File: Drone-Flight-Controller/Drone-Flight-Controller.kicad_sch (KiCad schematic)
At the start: 58 parts, among them J1 Screw_Terminal_01x02, J10 Conn_ARM_SWD_TagConnect_TC203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, J2 USB_B_Micro, J3 Screw_Terminal_01x03, J4 Screw_Terminal_01x03, J5 Screw_Terminal_01x03, J6 Screw_Terminal_01x03, J7 Screw_Terminal_01x02, J8 Screw_Terminal_01x03, SW1 SW_SPDT, U1 LMR51430, U2 NCP1117-3.3_SOT223, U3 STM32F401CBUx, U4 USBLC6-2SC6, U5 ADC101C021CIMK, U6 MPU-6050, U7 BMP280, Y1 16MHz

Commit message: forgot to save
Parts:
- removed H1, H2, H3, H4: MountingHole_Pad, MountingHole:MountingHole_4.3mm_M4_Pad_Via, symbol Mechanical:MountingHole_Pad
- removed SW1: SW_SPDT, Button_Switch_SMD:SW_SPDT_PCM12, symbol Switch:SW_SPDT
- added D2: LED, LED_SMD:LED_0402_1005Metric, symbol Device:LED
- added TP10, TP11, TP12, TP13, TP2, TP3, TP4, TP5, TP6, TP7, TP8, TP9: TestPoint, TestPoint:TestPoint_Pad_D1.0mm, symbol Connector:TestPoint
- C10: footprint Capacitor_THT:C_Radial_D4.0mm_H5.0mm_P1.50mm -> Capacitor_SMD:C_0504_1310Metric
- C2, C22, C23, C7: footprint Capacitor_THT:C_Radial_D4.0mm_H5.0mm_P1.50mm -> Capacitor_SMD:C_0402_1005Metric
- D1: footprint LED_THT:LED_D3.0mm -> LED_SMD:LED_0402_1005Metric
- D3: renamed from D2; footprint LED_THT:LED_D3.0mm -> LED_SMD:LED_0402_1005Metric
- R2, R3, R4, R5, R6, R7: footprint Resistor_THT:R_Axial_DIN0204_L3.6mm_D1.6mm_P7.62mm_Horizontal -> Resistor_SMD:R_0402_1005Metric
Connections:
- net +3.3V: now also R10.1
- net +5V: now also D2.2 (A)
- net BATVOLTAGE_ADDR: now also U3.31 (PA10)
- net BATVOLTAGE_SCL: now also U3.29 (PA8)
- net BATVOLTAGE_SDA: now also U3.30 (PA9)
- net GND: now also D2.1 (K)
- net SWCLK: now also J10.4 (SWCLK); no longer J10.2 (SWDIO)
- net SWDIO: now also J10.2 (SWDIO); no longer J10.4 (SWCLK)
- net UART_RX: now also J8.2 (Pin_2); no longer J8.3 (Pin_3)
- net UART_TX: now also J8.3 (Pin_3); no longer J8.2 (Pin_2)
- net at U3.18 (PB0): now also TP3.1
- net at U3.19 (PB1): now also TP4.1
- net at U3.2 (PC13): now also TP12.1
- net at U3.20 (PB2): now also TP5.1
- net at U3.21 (PB10): now also TP11.1
- net at U3.25 (PB12): now also TP10.1
- net at U3.26 (PB13): now also TP9.1
- net at U3.27 (PB14): now also TP8.1
- net at U3.28 (PB15): now also TP7.1
- net at U3.3 (PC14): now also TP13.1
- net at U3.38 (PA15): now also TP2.1
- net at U3.41 (PB5): now also TP6.1
- no-connect marks 7 -> 2

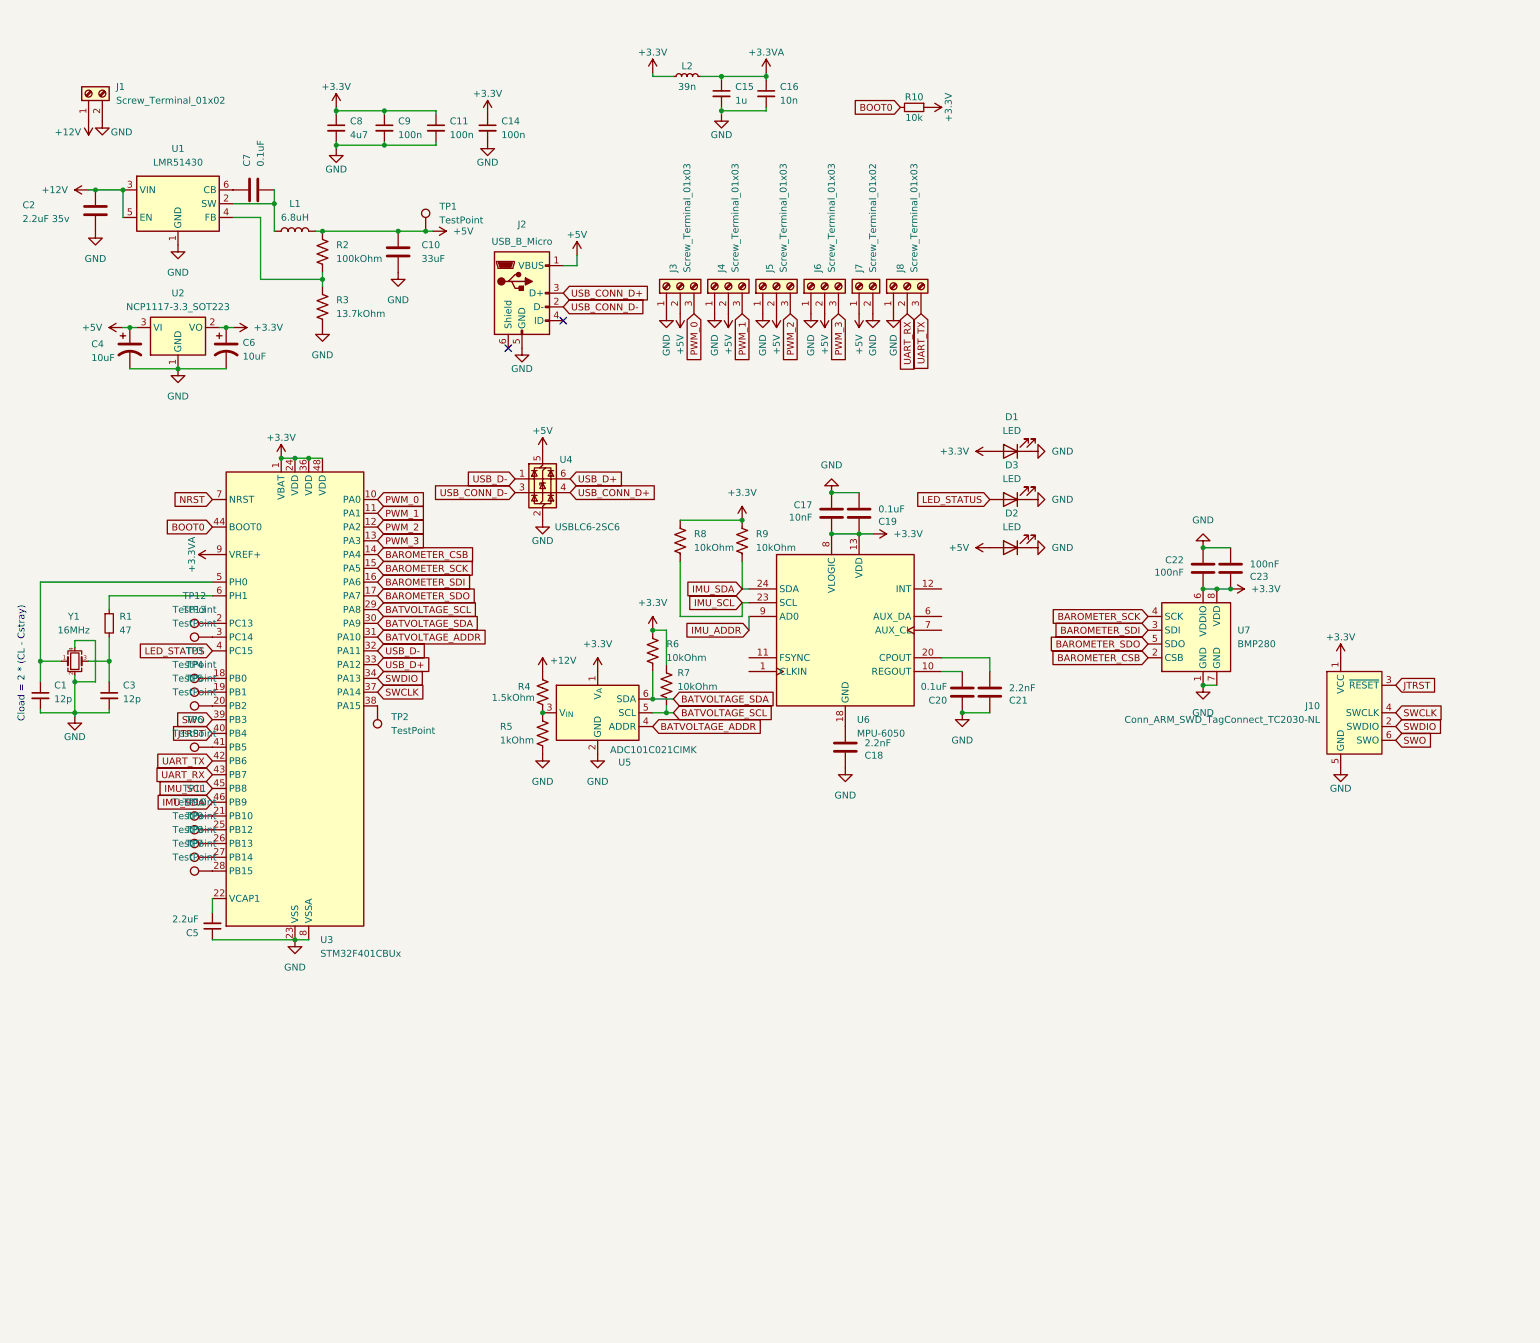
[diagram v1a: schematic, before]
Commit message: move to more powerful mcu
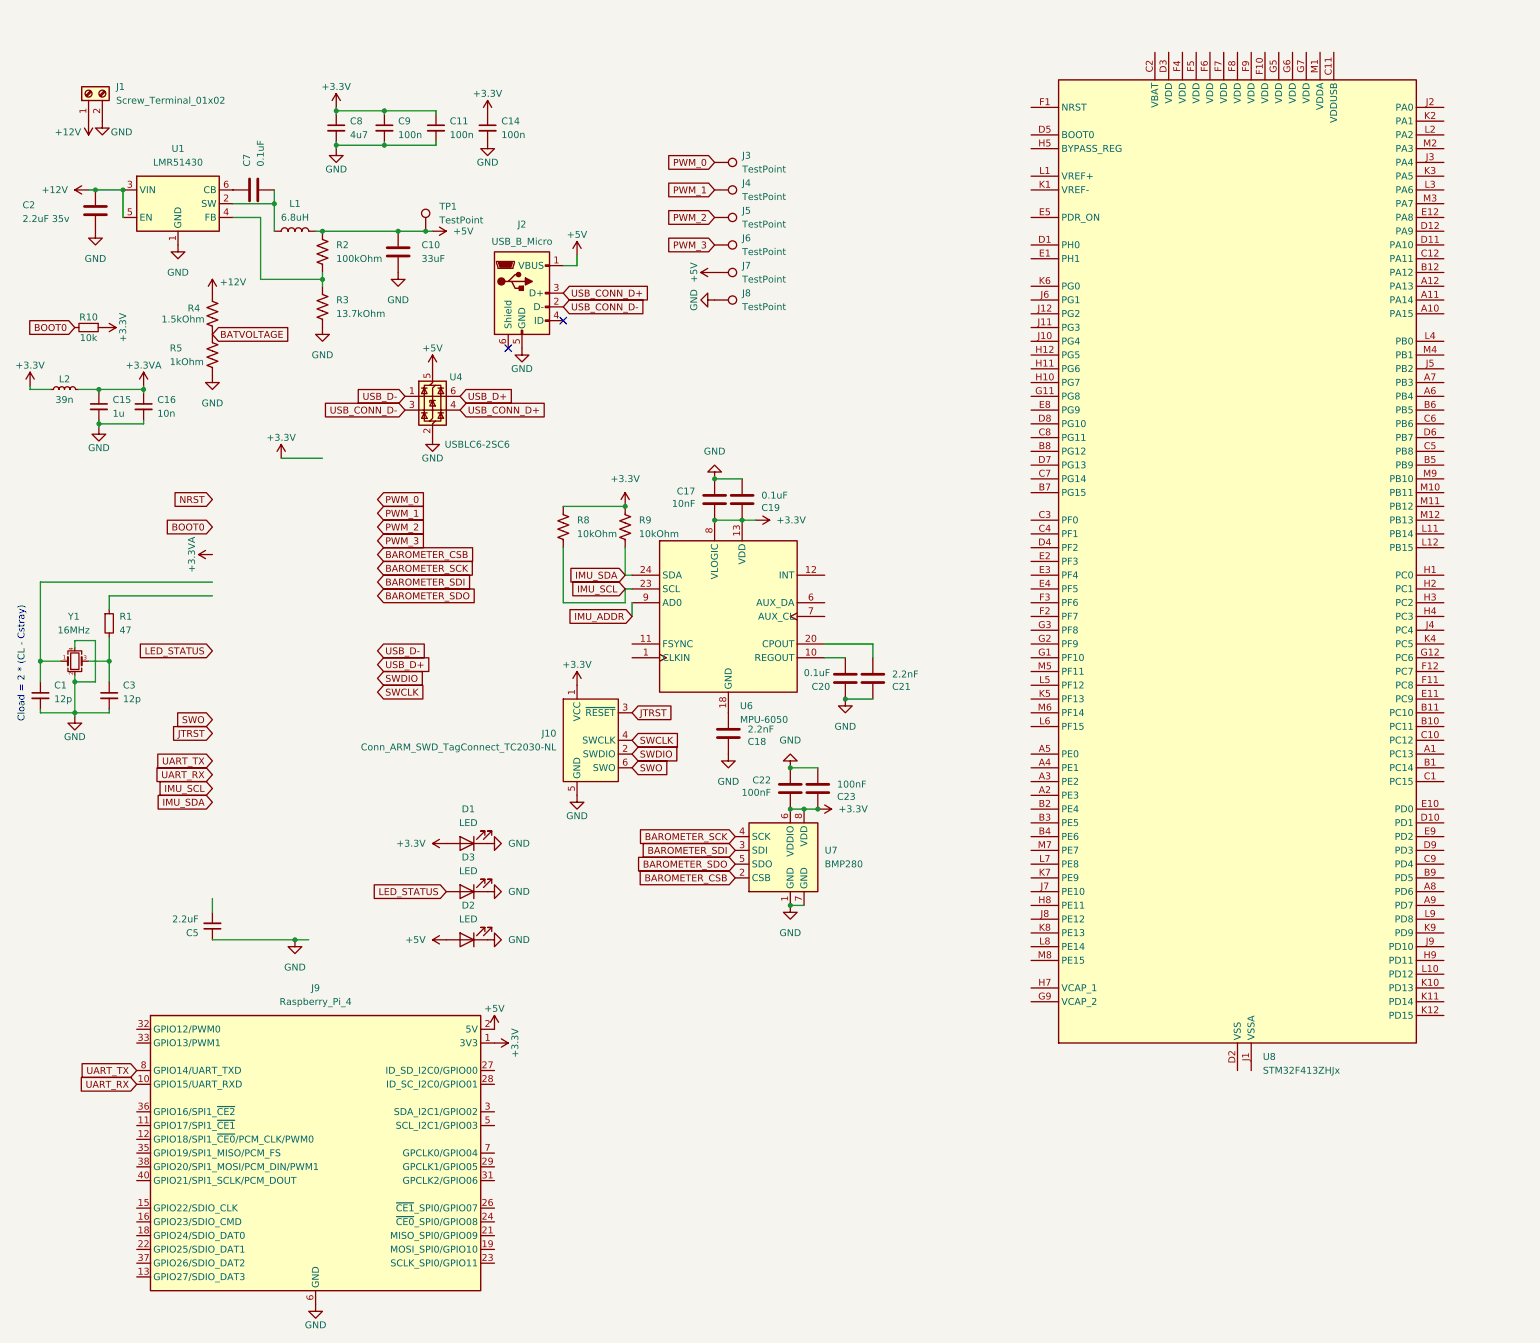
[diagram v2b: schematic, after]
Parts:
- removed C4, C6: 10uF, Capacitor_SMD:CP_Elec_3x5.3, symbol Device:C_Polarized_US
- removed J3, J4, J5, J6, J8: Screw_Terminal_01x03, TerminalBlock:TerminalBlock_Xinya_XY308-2.54-3P_1x03_P2.54mm_Horizontal, symbol Connector:Screw_Terminal_01x03
- removed J7: Screw_Terminal_01x02, TerminalBlock:TerminalBlock_Xinya_XY308-2.54-2P_1x02_P2.54mm_Horizontal, symbol Connector:Screw_Terminal_01x02
- removed R6, R7: 10kOhm, Resistor_SMD:R_0402_1005Metric, symbol Device:R_US
- removed TP10, TP11, TP12, TP13, TP2, TP3, TP4, TP5, TP6, TP7, TP8, TP9: TestPoint, TestPoint:TestPoint_Pad_D1.0mm, symbol Connector:TestPoint
- removed U2: NCP1117-3.3_SOT223, Package_TO_SOT_SMD:SOT-223-3_TabPin2, symbol Regulator_Linear:NCP1117-3.3_SOT223
- removed U3: STM32F401CBUx, Package_DFN_QFN:QFN-48-1EP_7x7mm_P0.5mm_EP3.5x3.5mm, symbol MCU_ST_STM32F4:STM32F401CBUx
- removed U5: ADC101C021CIMK, Package_TO_SOT_SMD:SOT-23-6, symbol Analog_ADC:ADC101C021CIMK
- added J3, J4, J5, J6, J7, J8: TestPoint, TestPoint:TestPoint_Pad_D2.0mm, symbol Connector:TestPoint
- added J9: Raspberry_Pi_4, Connector_PinHeader_2.54mm:PinHeader_2x20_P2.54mm_Vertical, symbol Connector:Raspberry_Pi_4
- added U8: STM32F413ZHJx, Package_BGA:UFBGA-144_10x10mm_Layout12x12_P0.8mm, symbol MCU_ST_STM32F4:STM32F413ZHJx
- R8, R9: footprint Resistor_THT:R_Axial_DIN0204_L3.6mm_D1.6mm_P7.62mm_Horizontal -> Resistor_SMD:R_0402_1005Metric
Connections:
- net +3.3V: now also J9.1 (3V3), J9.17 (3V3)
- net +5V: now also J7.1, J9.2 (5V), J9.4 (5V)
- net GND: now also J8.1, J9.14 (GND), J9.20 (GND), J9.25 (GND), J9.30 (GND), J9.34 (GND), J9.39 (GND), J9.6 (GND), J9.9 (GND)
- net PWM_0: now also J3.1
- net PWM_1: now also J4.1
- net PWM_2: now also J5.1
- net PWM_3: now also J6.1
- net UART_RX: now also J9.10 (GPIO15/UART_RXD)
- net UART_TX: now also J9.8 (GPIO14/UART_TXD)
- net BATVOLTAGE: now reaches R4.2, R5.1
- new net: U8.D2 (VSS), U8.E6 (VSS), U8.E7 (VSS), U8.G10 (VSS), U8.G4 (VSS), U8.G8 (VSS), U8.H6 (VSS)
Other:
- moved on the sheet: C15, C16, C17, C18, C19, C20, C21, C22, C23, D1, D2, D3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

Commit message: laid out pcb with new mcu
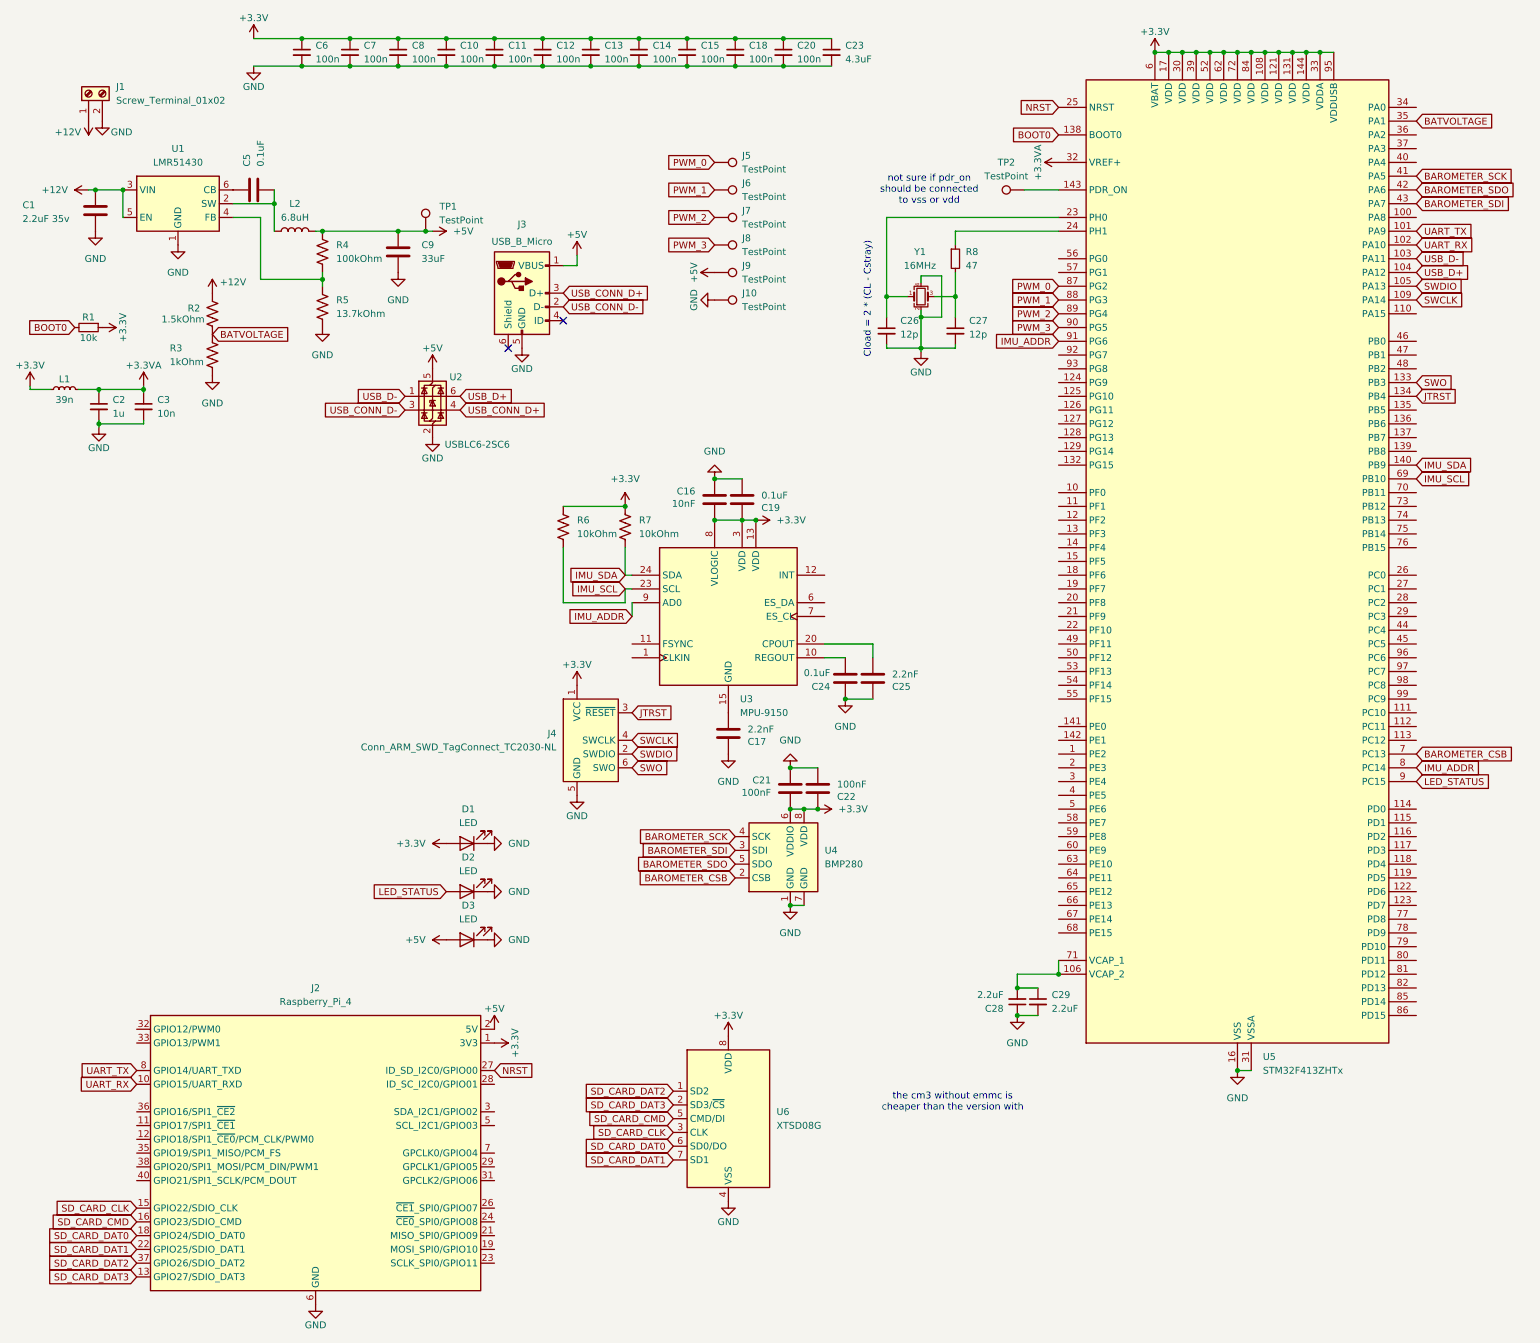
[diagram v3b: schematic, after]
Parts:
- removed C1, C3: 12p, Capacitor_SMD:C_0402_1005Metric, symbol Device:C_Small
- removed C9: 100n, Capacitor_SMD:C_0402_1005Metric, symbol Device:C_Small
- removed R1: 47, Resistor_SMD:R_0402_1005Metric, symbol Device:R_Small
- removed U6: MPU-6050, Sensor_Motion:InvenSense_QFN-24_4x4mm_P0.5mm, symbol Sensor_Motion:MPU-6050
- removed U8: STM32F413ZHJx, Package_BGA:UFBGA-144_10x10mm_Layout12x12_P0.8mm, symbol MCU_ST_STM32F4:STM32F413ZHJx
- added C10, C12, C13, C15, C18, C20, C6, C7: 100n, Capacitor_SMD:C_0402_1005Metric, symbol Device:C_Small
- added C23: 4.3uF, Capacitor_SMD:C_0402_1005Metric, symbol Device:C_Small
- added C26, C27: 12p, Capacitor_SMD:C_0402_1005Metric, symbol Device:C_Small
- added C29: 2.2uF, Capacitor_SMD:C_0402_1005Metric, symbol Device:C_Small
- added R8: 47, Resistor_SMD:R_0402_1005Metric, symbol Device:R_Small
- added TP2: TestPoint, TestPoint:TestPoint_Pad_D1.0mm, symbol Connector:TestPoint
- added U3: MPU-9150, Sensor_Motion:InvenSense_QFN-24_4x4mm_P0.5mm, symbol Sensor_Motion:MPU-9150
- added U5: STM32F413ZHTx, Package_QFP:LQFP-144_20x20mm_P0.5mm, symbol MCU_ST_STM32F4:STM32F413ZHTx
- added U6: XTSD08G, Package_LGA:LGA-8_8x6mm_P1.27mm, symbol Memory_Flash:XTSD08G
- C8: value 4u7 -> 100n; footprint Capacitor_SMD:C_0603_1608Metric -> Capacitor_SMD:C_0402_1005Metric; LCSC Part # C19666 -> C1525
- renumbered C2 to C1, C17 to C16, C18 to C17, C15 to C2, C22 to C21, C23 to C22, C20 to C24, C21 to C25, C5 to C28, C16 to C3, C7 to C5, C10 to C9, D3 to D2, D2 to D3, J8 to J10, J9 to J2, J2 to J3, J10 to J4, J3 to J5, J4 to J6, J5 to J7, J6 to J8, J7 to J9, L2 to L1, L1 to L2, R10 to R1, R4 to R2, R5 to R3, R2 to R4, R3 to R5, R8 to R6, R9 to R7, U4 to U2, U7 to U4
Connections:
- net +3.3V: now also C10.1, C12.1, C13.1, C15.1, C18.1, C20.1, C23.1, C6.1, C7.1, U3.13 (VDD), U3.3 (VDD), U3.8 (VLOGIC), U5.108 (VDD), U5.121 (VDD), U5.131 (VDD), U5.144 (VDD), U5.17 (VDD), U5.30 (VDD), U5.33 (VDDA), U5.39 (VDD), U5.52 (VDD), U5.6 (VBAT), U5.62 (VDD), U5.72 (VDD), U5.84 (VDD), U5.95 (VDDUSB), U6.8 (VDD)
- net +3.3VA: now also U5.32 (VREF+)
- net BAROMETER_CSB: now also U5.7 (PC13)
- net BAROMETER_SCK: now also U5.41 (PA5)
- net BAROMETER_SDI: now also U5.43 (PA7)
- net BAROMETER_SDO: now also U5.42 (PA6)
- net BATVOLTAGE: now also U5.35 (PA1)
- net BOOT0: now also U5.138 (BOOT0)
- net GND: now also C10.2, C12.2, C13.2, C15.2, C18.2, C20.2, C23.2, C26.2, C27.2, C29.2, C6.2, C7.2, U5.107 (VSS), U5.120 (VSS), U5.130 (VSS), U5.16 (VSS), U5.31 (VSSA), U5.38 (VSS), U5.51 (VSS), U5.61 (VSS), U5.83 (VSS), U5.94 (VSS), U6.4 (VSS)
- net IMU_ADDR: now also U3.9 (AD0), U5.8 (PC14), U5.91 (PG6)
- net IMU_SCL: now also U3.23 (SCL), U5.69 (PB10)
- net IMU_SDA: now also U3.24 (SDA), U5.140 (PB9)
- net JTRST: now also U5.134 (PB4)
- net LED_STATUS: now also U5.9 (PC15)
- net NRST: now also J2.27 (ID_SD_I2C0/GPIO00), U5.25 (NRST)
- net PWM_0: now also U5.87 (PG2)
- net PWM_1: now also U5.88 (PG3)
- net PWM_2: now also U5.89 (PG4)
- net PWM_3: now also U5.90 (PG5)
- net SWCLK: now also U5.109 (PA14)
- net SWDIO: now also U5.105 (PA13)
- net SWO: now also U5.133 (PB3)
- net UART_RX: now also U5.102 (PA10)
- net UART_TX: now also U5.101 (PA9)
- net USB_D+: now also U5.104 (PA12)
- net USB_D-: now also U5.103 (PA11)
- net at Y1.3: now also C27.1, R8.2
- net at Y1.1: now also C26.1, U5.23 (PH0)
- net at C17.1: now also U3.15 (GND), U3.17 (GND), U3.18 (GND)
- net SD_CARD_DAT3: now reaches J2.13 (GPIO27/SDIO_DAT3)
- net SD_CARD_DAT3: now also U6.2 (SD3/~{CS})
- net SD_CARD_CLK: now reaches J2.15 (GPIO22/SDIO_CLK)
- net SD_CARD_CLK: now also U6.3 (CLK)
- net SD_CARD_CMD: now reaches J2.16 (GPIO23/SDIO_CMD)
- net SD_CARD_CMD: now also U6.5 (CMD/DI)
- net SD_CARD_DAT0: now reaches J2.18 (GPIO24/SDIO_DAT0)
- net SD_CARD_DAT0: now also U6.6 (SD0/DO)
- net SD_CARD_DAT1: now reaches J2.22 (GPIO25/SDIO_DAT1)
- net SD_CARD_DAT1: now also U6.7 (SD1)
- net SD_CARD_DAT2: now reaches J2.37 (GPIO26/SDIO_DAT2)
- net SD_CARD_DAT2: now also U6.1 (SD2)
- net at C24.2: now also U3.10 (REGOUT)
- net at C28.2: now also C29.1, U5.106 (VCAP_2), U5.71 (VCAP_1)
- net at C25.1: now also U3.20 (CPOUT)
- new net: TP2.1, U5.143 (PDR_ON)
- new net: R8.1, U5.24 (PH1)
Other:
- note added: "not sure if pdr_on should be connected to vss or vdd"
- note added: "the cm3 without emmc is cheaper than the version with"
- moved on the sheet: C28
